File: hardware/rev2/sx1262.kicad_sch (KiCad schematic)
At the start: 31 parts, among them U1 SX1262IMLTRT, U2 PE4259, Y1 TCXO 32MHz

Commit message: did some schematic stuff
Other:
- note added: "DigiKey/RS?"

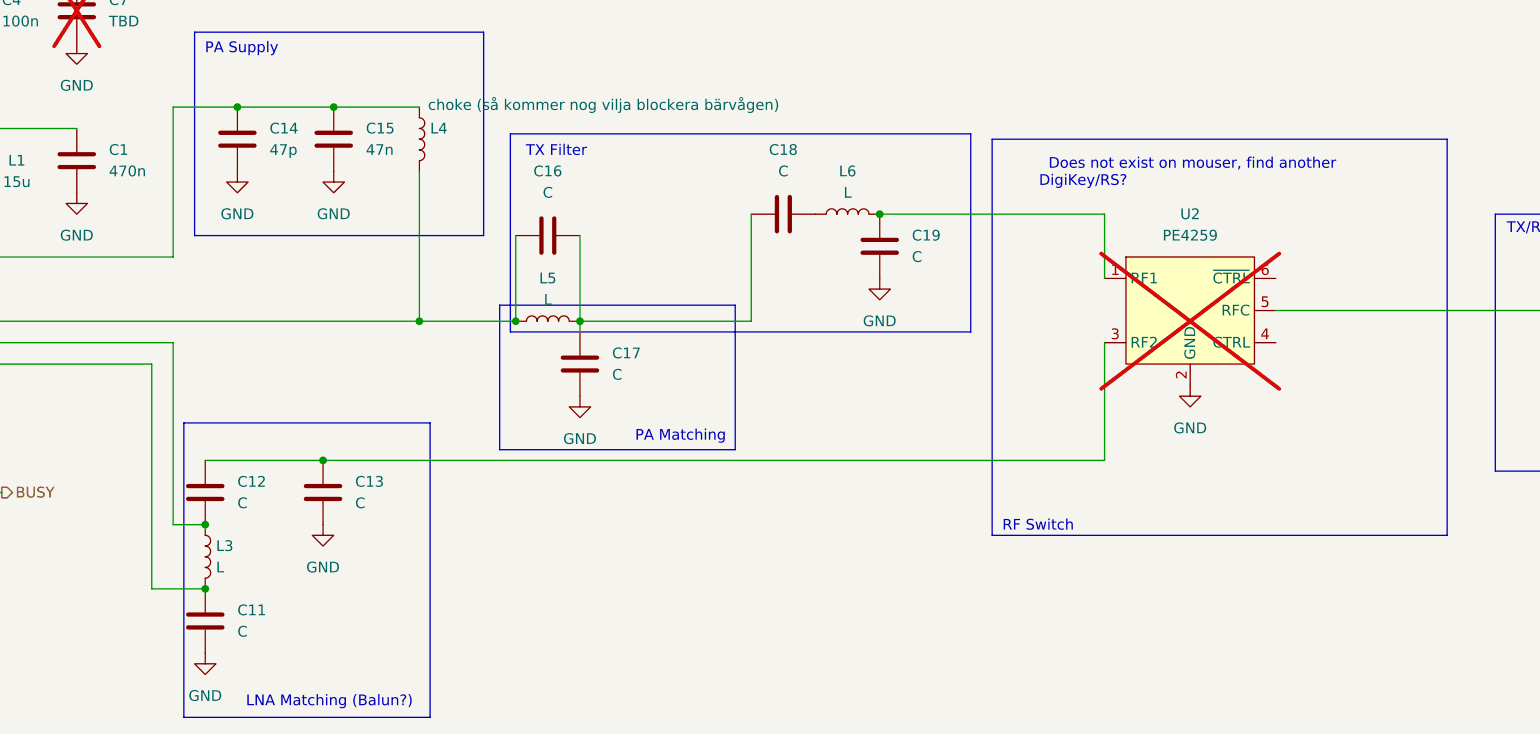
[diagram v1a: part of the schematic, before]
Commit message: board stackup + design rules + initial pcb
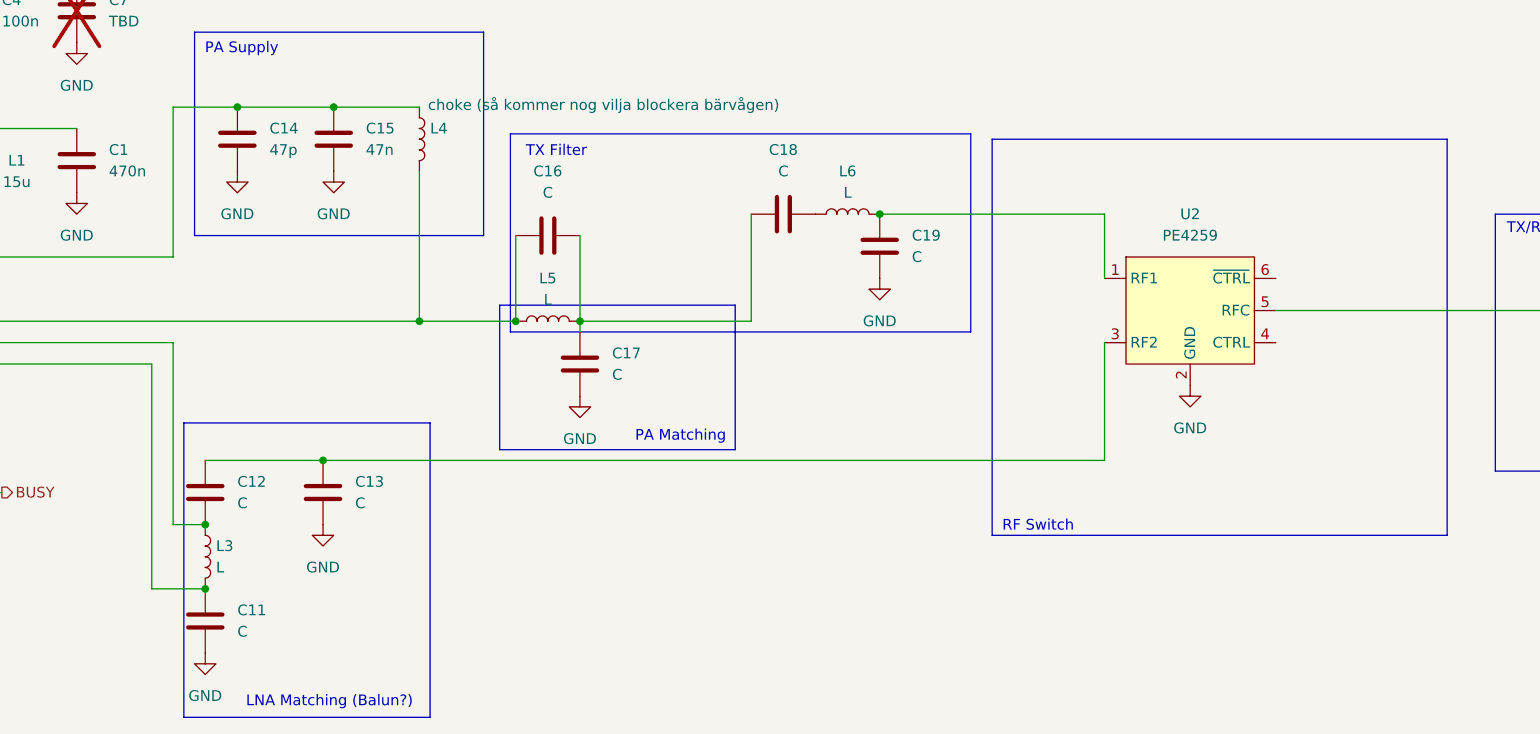
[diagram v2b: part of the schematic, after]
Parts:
- U1: Digikey Part Number (none) -> SX1262IMLTRTCT-ND
- U2: Digikey Part Number (none) -> 1046-1011-1-ND; Mouser Part Number (none) -> -; now fitted
- Y1: Digikey Part Number (none) -> SX1262IMLTRTTR-ND
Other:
- note removed: "DigiKey/RS?"
- note removed: "Does not exist on mouser, find another"

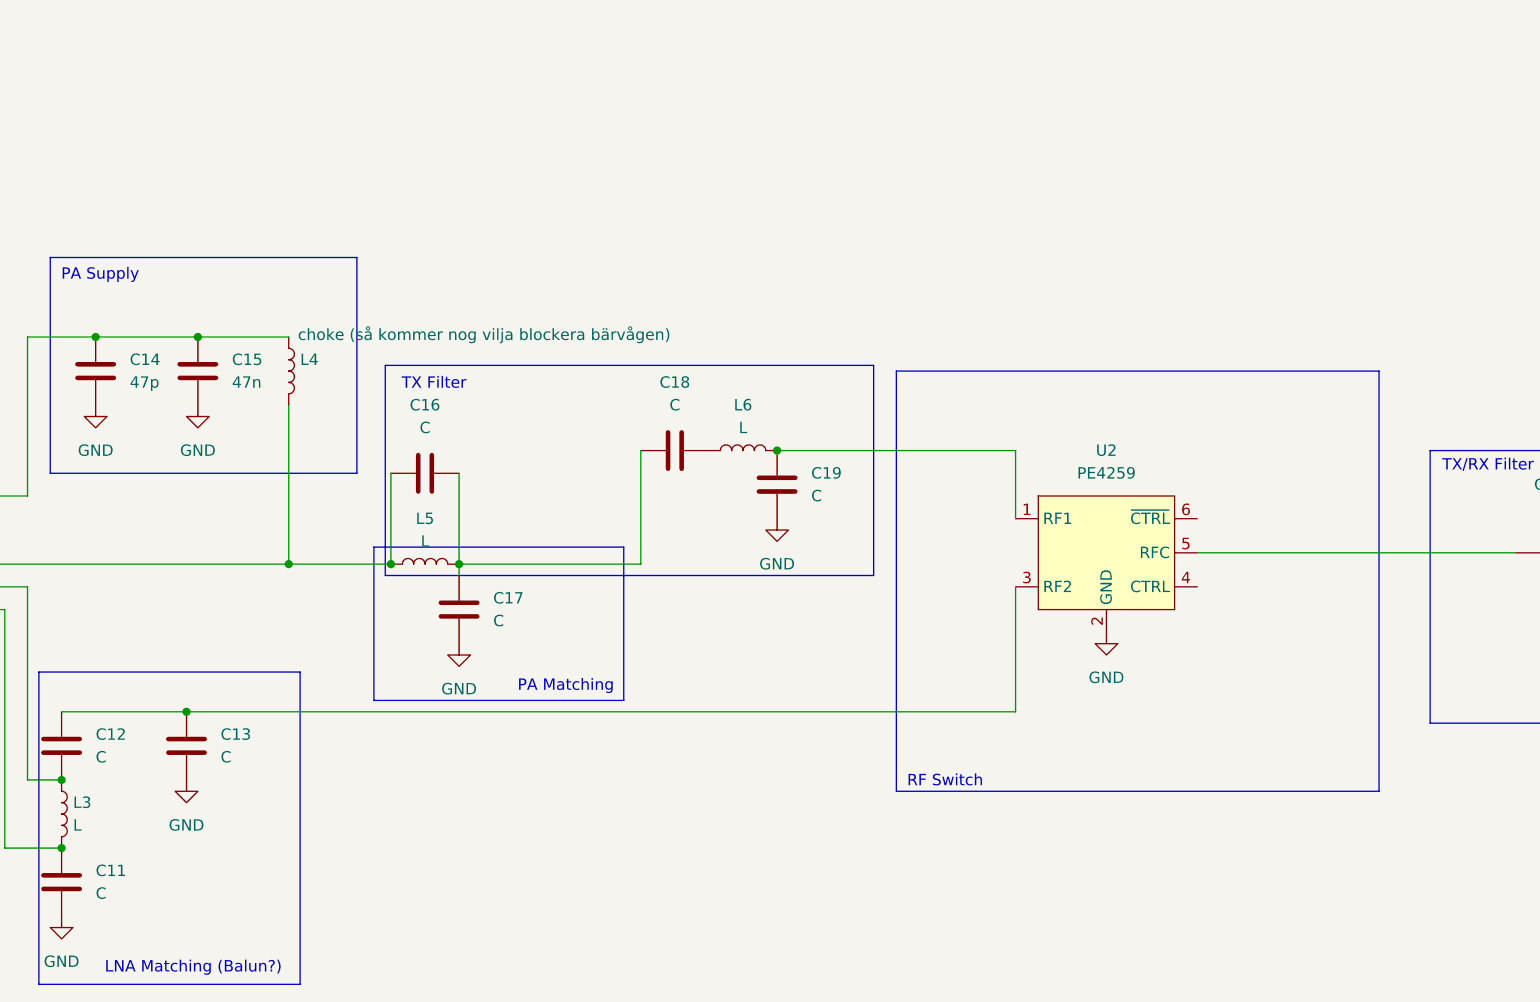
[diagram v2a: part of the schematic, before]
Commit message: found _one_ component value maybe
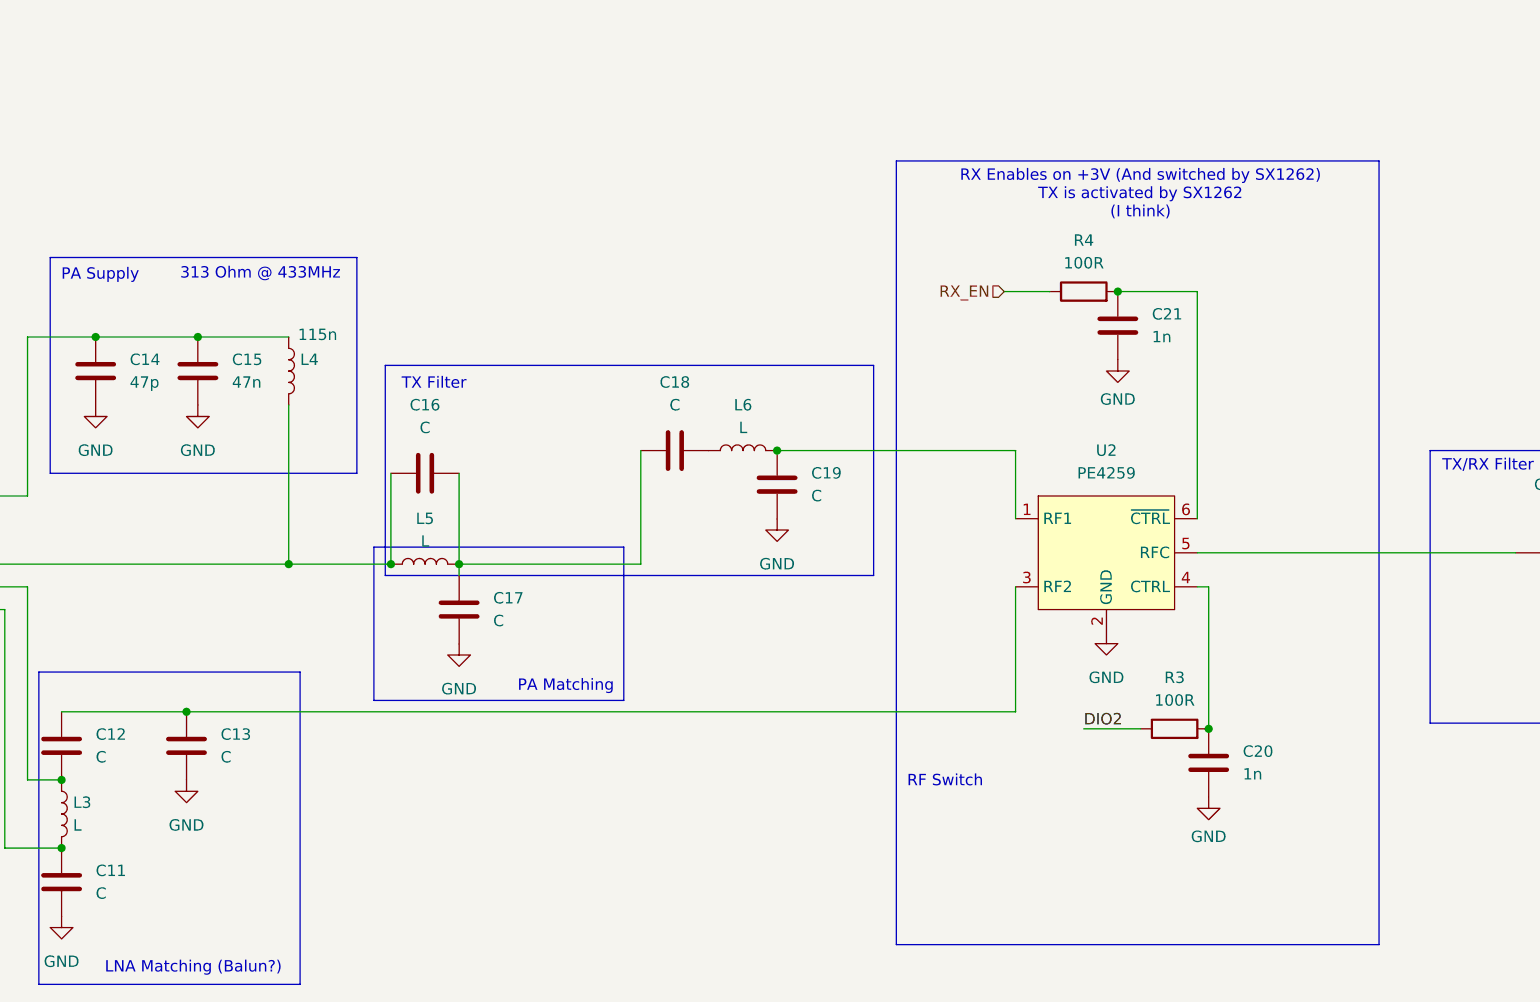
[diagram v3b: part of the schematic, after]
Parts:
- added C20, C21: 1n, symbol Device:C
- added R3, R4: 100R, symbol Device:R
- L4: value choke (så kommer nog vilja blockera bärvågen) -> 115n
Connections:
- net DIO2: now also R3.1
- net GND: now also C20.2, C21.2
- net at U2.4 (CTRL): now also C20.1, R3.2
- net at U2.6 (~{CTRL}): now also C21.1, R4.2
- new net RX_EN: R4.1
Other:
- note added: "313 Ohm @ 433MHz"
- note added: "RX Enables on +3V (And switched by SX1262) TX is activated by SX1262 (I think)"

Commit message: added context
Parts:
- C10, C12, C18: value C -> DC Block
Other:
- note added: "Switch Matching & DC-Block"
- moved on the sheet: C13

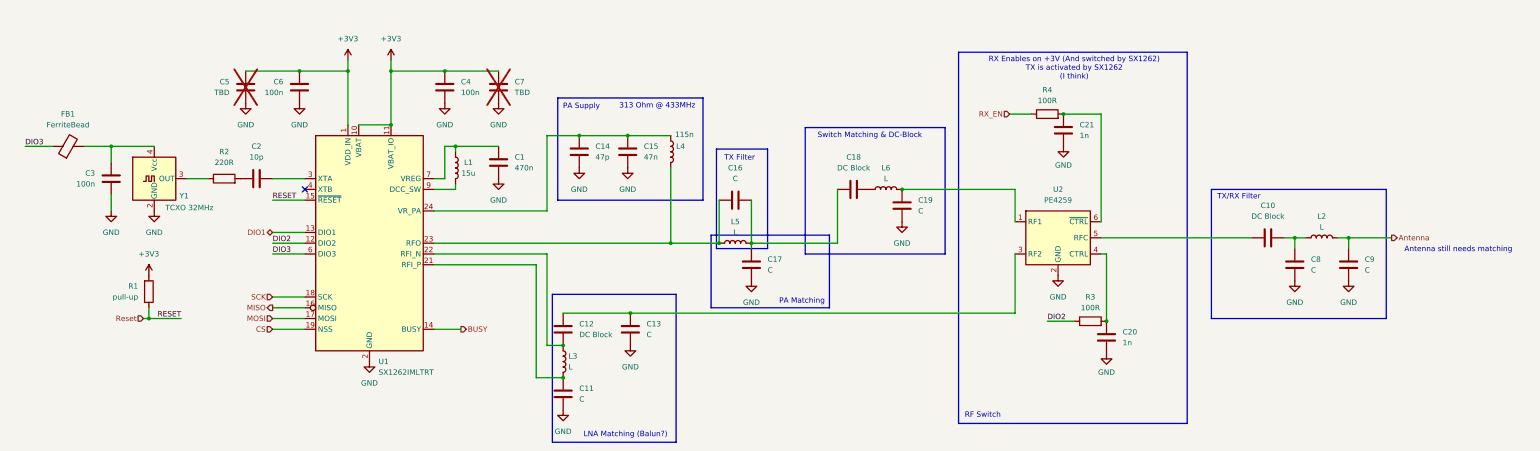
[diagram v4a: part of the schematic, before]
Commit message: added power, net classes and some antenna stuff
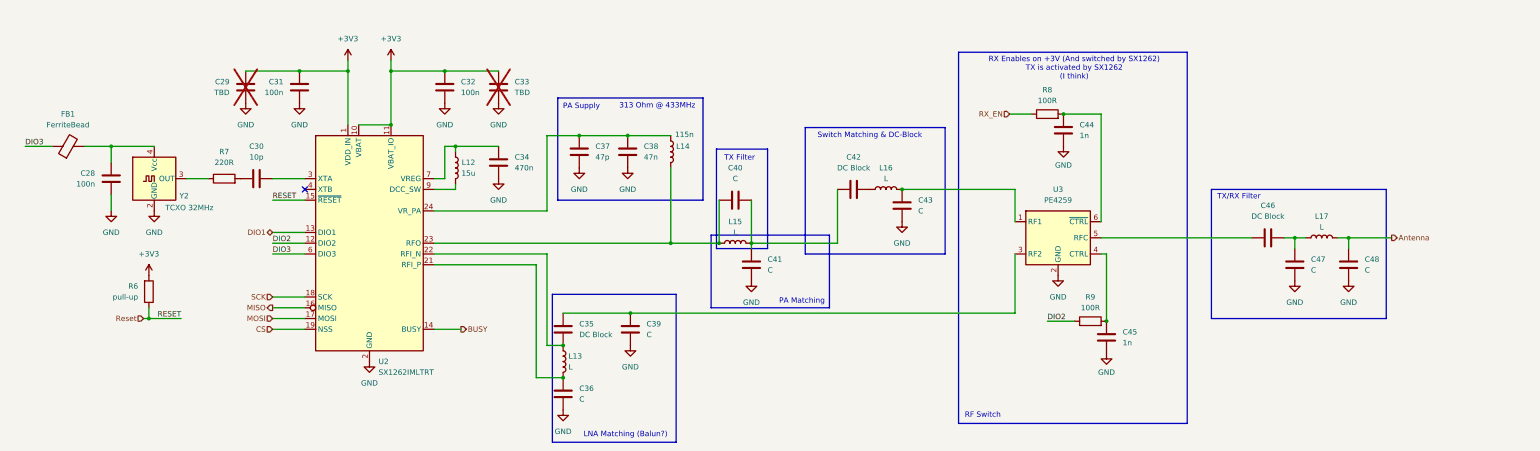
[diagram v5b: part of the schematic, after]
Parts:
- renumbered C3 to C28, C5 to C29, C2 to C30, C6 to C31, C4 to C32, C7 to C33, C1 to C34, C12 to C35, C11 to C36, C14 to C37, C15 to C38, C13 to C39, C16 to C40, C17 to C41, C18 to C42, C19 to C43, C21 to C44, C20 to C45, C10 to C46, C8 to C47, C9 to C48, L1 to L12, L3 to L13, L4 to L14, L5 to L15, L6 to L16, L2 to L17, R1 to R6, R2 to R7, R4 to R8, R3 to R9, U1 to U2, U2 to U3, Y1 to Y2
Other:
- note removed: "Antenna still needs matching"
